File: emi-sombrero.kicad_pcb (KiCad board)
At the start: 4 copper layers, 65 x 56.5 mm, 112 parts, among them J1 WE_687130149022, J2 Conn_02x20_Odd_Even, U1 74LVC1G29, U10 74LVC1G125, U2 LD1117S50TR_SOT223, U3 LD1117S33TR_SOT223, U4 ISU0205S15, U5 ISU0205S15, U6 LT3032, U7 LT3032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

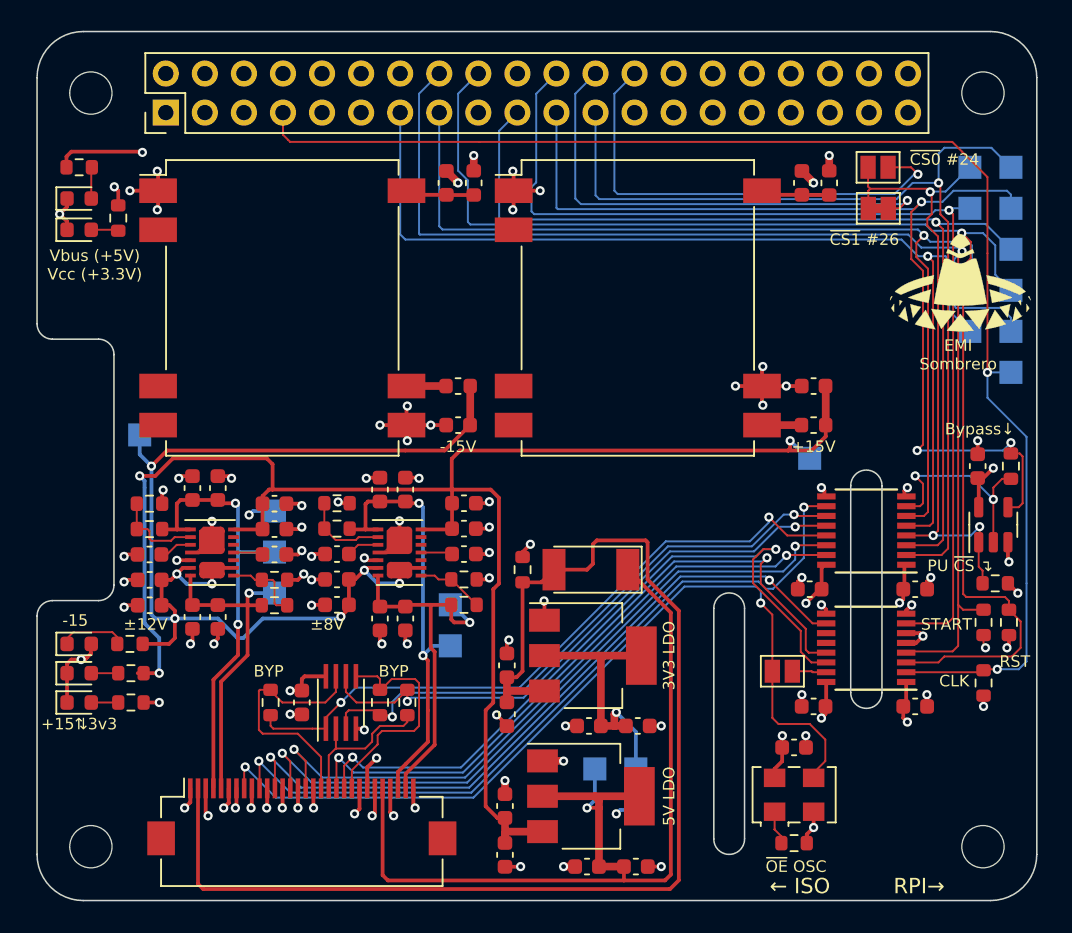
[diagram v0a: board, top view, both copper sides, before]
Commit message: Add more testpoints, make DRDY optionally open collector.
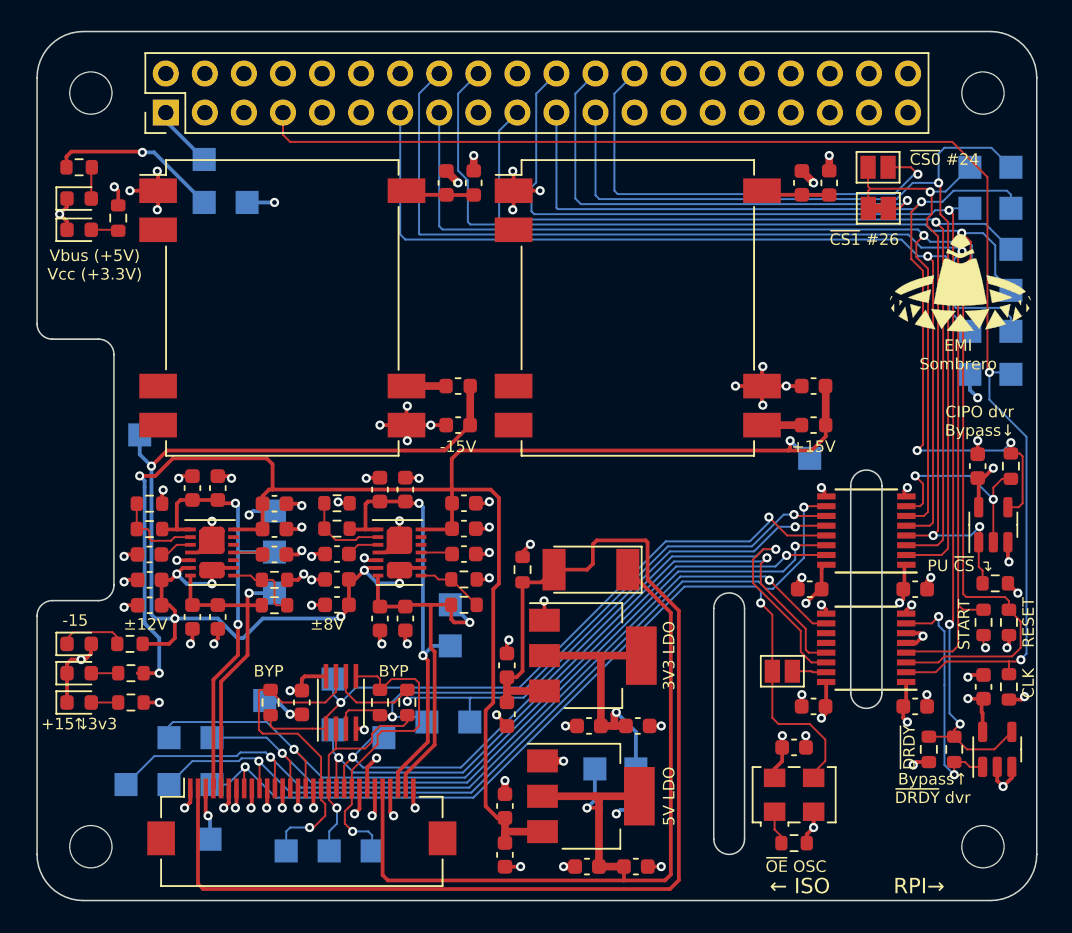
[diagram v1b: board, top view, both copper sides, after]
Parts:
- added C40: 100n, Capacitor_SMD:C_0603_1608Metric, F.Cu at (177.7, 103.4)
- added R24: DNP, Resistor_SMD:R_0603_1608Metric, F.Cu at (175.8, 107.4)
- added R25: 10k, Resistor_SMD:R_0603_1608Metric, F.Cu at (174.1, 107.4)
- added TP21: TestPoint_Small, TestPoint:TestPoint_Pad_1.5x1.5mm, B.Cu at (124.7, 106.7)
- added TP22: TestPoint_Small, TestPoint:TestPoint_Pad_1.5x1.5mm, B.Cu at (127.5, 106.7)
- added TP23: TestPoint_Small, TestPoint:TestPoint_Pad_1.5x1.5mm, B.Cu at (135.4, 102.9)
- added TP24: TestPoint_Small, TestPoint:TestPoint_Pad_1.5x1.5mm, B.Cu at (144.3, 105.7)
- added TP25: TestPoint_Small, TestPoint:TestPoint_Pad_1.5x1.5mm, B.Cu at (141.5, 105.7)
- added TP26: TestPoint_Small, TestPoint:TestPoint_Pad_1.5x1.5mm, B.Cu at (124.7, 109.7)
- added TP27: TestPoint_Small, TestPoint:TestPoint_Pad_1.5x1.5mm, B.Cu at (127.5, 109.7)
- added TP28: TestPoint_Small, TestPoint:TestPoint_Pad_1.5x1.5mm, B.Cu at (138.7, 106.7)
- added TP29: TestPoint_Small, TestPoint:TestPoint_Pad_1.5x1.5mm, B.Cu at (135.4, 106.2)
- added TP30: TestPoint_Small, TestPoint:TestPoint_Pad_1.5x1.5mm, B.Cu at (121.9, 109.7)
- added TP31: TestPoint_Small, TestPoint:TestPoint_Pad_1.5x1.5mm, B.Cu at (132.3, 114.0)
- added TP32: TestPoint_Small, TestPoint:TestPoint_Pad_1.5x1.5mm, B.Cu at (135.1, 114.0)
- added TP33: TestPoint_Small, TestPoint:TestPoint_Pad_1.5x1.5mm, B.Cu at (137.9, 114.0)
- added TP34: TestPoint_Small, TestPoint:TestPoint_Pad_1.5x1.5mm, B.Cu at (130.9, 104.3)
- added TP35: TestPoint_Small, TestPoint:TestPoint_Pad_1.5x1.5mm, B.Cu at (127.4, 113.3)
- added TP36: TestPoint_Small, TestPoint:TestPoint_Pad_1.5x1.5mm, B.Cu at (129.8, 71.9)
- added TP37: TestPoint_Small, TestPoint:TestPoint_Pad_1.5x1.5mm, B.Cu at (176.8, 83.1)
- added TP38: TestPoint_Small, TestPoint:TestPoint_Pad_1.5x1.5mm, B.Cu at (127.0, 69.1)
- added TP39: TestPoint_Small, TestPoint:TestPoint_Pad_1.5x1.5mm, B.Cu at (127.0, 71.9)
- added U11: 74LVC1G125, Package_TO_SOT_SMD:SOT-23-5, F.Cu at (178.6, 107.4)
- moved R17 1.67 mm to (179.3, 103.4)
- moved TP17 0.13 mm to (179.5, 83.1)
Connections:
- U9 pad 7: /DRDY_RPI -> Net-(R24-Pad1)
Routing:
- net Net-(R24-Pad1): track 0.00 -> 15.8 mm, vias 0 -> 2
- net /DRDY_RPI: track 68.2 -> 79.5 mm, vias 1 -> 3
- net /DRDY: track 46.0 -> 56.4 mm
- net /SCK: track 44.1 -> 53.3 mm
- net VCC: track 11.7 -> 20.0 mm, vias 6 -> 8
- net GND: track 22.5 -> 30.0 mm, vias 18 -> 22
- net /CIPO: track 49.5 -> 56.1 mm
- net /~{CS1}: track 16.0 -> 22.1 mm, vias 0 -> 1
- net /~{CS3}: track 15.2 -> 20.7 mm, vias 0 -> 1
- net VBUS: track 61.9 -> 67.3 mm
- net /COPI: track 45.4 -> 50.4 mm
- net /~{CS2}: track 10.2 -> 14.7 mm, vias 0 -> 1
- net GND1: track 85.8 -> 89.4 mm
- net /CLK: track 57.0 -> 59.6 mm
- net /~{RESET}: track 46.9 -> 49.4 mm
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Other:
- board text added: "+3.3V +5V"
- board text added: "Bypass↑ ~{DRDY} dvr"
- board text added: "CIPO dvr Bypass↓"
- board text added: "CLK CIPO"
- board text added: "CLK GND"
- board text added: "COPI SCK"
- board text added: "CS A0/A1"
- board text added: "DRDY"
- board text added: "GND"
- board text added: "GND VBUS"
- board text added: "Isolated ↓"
- board text added: "RESET"
- board text added: "Raspi ↑"
- board text added: "VCC"
- board text added: "~{CS3} ~{CS2} ~{CS1}"
- board text added: "~{CS}"
- board text added: "~{DRDY}"
- board text added: "~{RESET}"
- board text removed: "+3.3V +5V GND"
- board text removed: "Bypass↓"
- board text removed: "RST"
